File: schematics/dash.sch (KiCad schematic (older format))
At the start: 29 parts, among them J1 BATT_CONN, J2 EXTERNAL_TRIGGER, J3 USB_OTG, SW1 SW_Push, U1 ESP-12E, U2 ch340g, U3 MCP73833, U4 HT7333, Y1 12Mhz

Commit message: [enh] Change capacitor value to match ceramic capacitor availability
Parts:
- removed C1: 470uF, Capacitors_SMD:C_1206_HandSoldering, symbol C
- added C1: 220uF, Capacitors_SMD:C_1206_HandSoldering, symbol C_Small
- C7: footprint Capacitors_Tantalum_SMD:CP_Tantalum_Case-A_EIA-3216-18_Hand -> Capacitors_SMD:C_1206_HandSoldering
- C9: value 470uF -> 220uF; footprint Capacitors_Tantalum_SMD:CP_Tantalum_Case-D_EIA-7343-31_Hand -> Capacitors_SMD:C_1206_HandSoldering
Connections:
- net GND: now also C1.2
- net at C7.2, J1.2 (P2), U3.10 (VBAT)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: now also C1.1
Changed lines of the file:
@@
-$EndComp
-$Comp
-L C C1
-U 1 1 5960EA3A
-P 8800 2150
-F 0 "C1" H 8825 2250 50  0000 L CNN
-F 1 "470uF" H 8825 2050 50  0000 L CNN
-F 2 "Capacitors_SMD:C_1206_HandSoldering" H 8838 2000 50  0001 C CNN
-F 3 "" H 8800 2150 50  0001 C CNN
-	1    8800 2150
-	1    0    0    -1
 $EndComp
 $Comp
@@
 F 0 "C7" V 8250 2000 50  0000 L CNN
 F 1 "1uF" V 8250 2200 50  0000 L CNN
-F 2 "Capacitors_Tantalum_SMD:CP_Tantalum_Case-A_EIA-3216-18_Hand" H 8200 2150 50  0001 C CNN
+F 2 "Capacitors_SMD:C_1206_HandSoldering" H 8200 2150 50  0001 C CNN
 F 3 "" H 8200 2150 50  0001 C CNN
 	1    8200 2150
@@
 P 10000 2150
 F 0 "C9" H 10010 2220 50  0000 L CNN
-F 1 "470uF" H 10010 2070 50  0000 L CNN
-F 2 "Capacitors_Tantalum_SMD:CP_Tantalum_Case-D_EIA-7343-31_Hand" H 10000 2150 50  0001 C CNN
+F 1 "220uF" H 10010 2070 50  0000 L CNN
+F 2 "Capacitors_SMD:C_1206_HandSoldering" H 10000 2150 50  0001 C CNN
 F 3 "" H 10000 2150 50  0001 C CNN
 	1    10000 2150
@@
 Connection ~ 8800 1900
 Wire Wire Line
-	8800 2400 8800 2300
-Wire Wire Line
-	8800 1900 8800 2000
+	8800 2250 8800 2400
+Wire Wire Line
+	8800 1900 8800 2050
 Wire Wire Line
 	5750 4550 5350 4550
@@
 	1    0    0    -1
 $EndComp
+$Comp
+L C_Small C1
+U 1 1 59C67224
+P 8800 2150
+F 0 "C1" H 8810 2220 50  0000 L CNN
+F 1 "220uF" H 8810 2070 50  0000 L CNN
+F 2 "Capacitors_SMD:C_1206_HandSoldering" H 8800 2150 50  0001 C CNN
+F 3 "" H 8800 2150 50  0001 C CNN
+	1    8800 2150
+	1    0    0    -1
+$EndComp

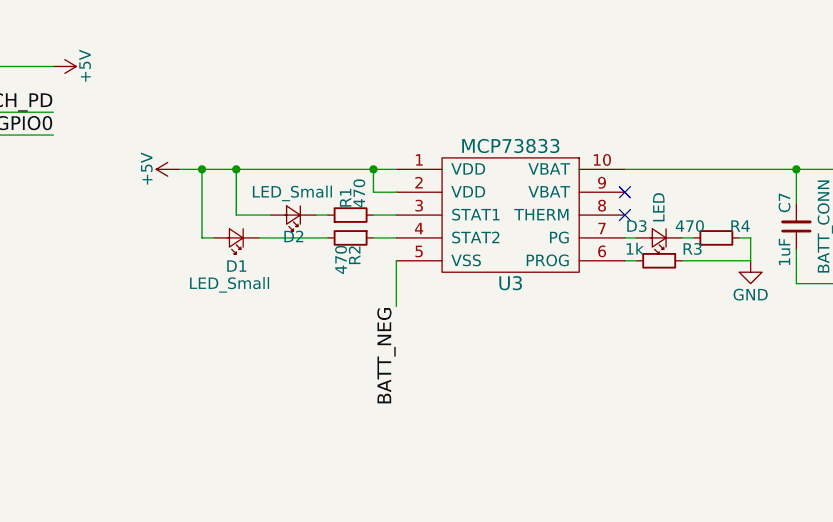
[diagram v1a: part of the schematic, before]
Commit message: [enh] Redesigned project to take less space
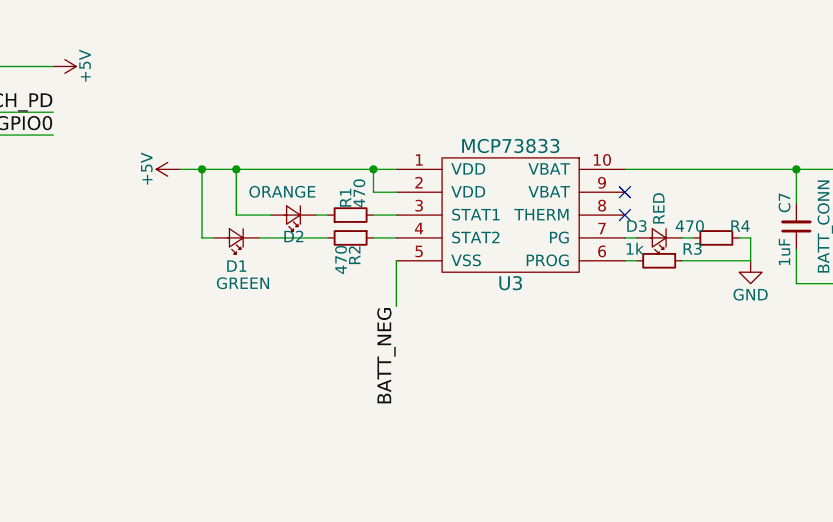
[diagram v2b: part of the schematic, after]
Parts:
- D1: value LED_Small -> GREEN
- D2: value LED_Small -> ORANGE
- D3: value LED -> RED
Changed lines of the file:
@@
 P 6000 2100
 F 0 "D2" H 5950 2225 50  0000 L TNN
-F 1 "LED_Small" H 5825 2000 50  0000 L CNN
+F 1 "ORANGE" H 5900 2000 50  0000 L CNN
 F 2 "LEDs:LED_1206" V 6000 2100 50  0001 C CNN
 F 3 "" V 6000 2100 50  0001 C CNN
@@
 P 5750 2200
 F 0 "D1" H 5700 2325 50  0000 L CNN
-F 1 "LED_Small" H 5600 2400 50  0000 L CNN
+F 1 "GREEN" H 5600 2400 50  0000 L CNN
 F 2 "LEDs:LED_1206" V 5750 2200 50  0001 C CNN
 F 3 "" V 5750 2200 50  0001 C CNN
@@
 P 7600 2200
 F 0 "D3" H 7650 2150 50  0000 L CNN
-F 1 "LED" V 7600 2000 50  0000 L CNN
+F 1 "RED" V 7600 2000 50  0000 L CNN
 F 2 "LEDs:LED_1206" V 7600 2200 50  0001 C CNN
 F 3 "" V 7600 2200 50  0001 C CNN

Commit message: [add] Pinout
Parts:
- added J4, J5: Conn_01x08, Pin_Headers:Pin_Header_Straight_1x08_Pitch2.54mm, symbol Conn_01x08
- U4: footprint TO_SOT_Packages_SMD:SOT89-3_Housing_Handsoldering -> sot:SOT89
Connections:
- net +3V3: now also J4.1 (Pin_1)
- net CH_PD: now also J4.6 (Pin_6)
- net GND: now also J5.8 (Pin_8)
- net GPIO0: now also J5.5 (Pin_5)
- net GPIO15: now also J5.7 (Pin_7)
- net GPIO2: now also J5.6 (Pin_6)
- net RXD: now also J5.2 (Pin_2)
- net TXD: now also J5.1 (Pin_1)
- net GPIO4: now reaches U1.13 (GPIO4)
- net GPIO4: now also J5.4 (Pin_4)
- net GPIO5: now reaches U1.14 (GPIO5)
- net GPIO5: now also J5.3 (Pin_3)
- net ADC: now reaches U1.2 (ADC)
- net ADC: now also J4.7 (Pin_7)
- net GPIO14: now reaches U1.5 (GPIO14)
- net GPIO14: now also J4.4 (Pin_4)
- net GPIO12: now reaches U1.6 (GPIO12)
- net GPIO12: now also J4.3 (Pin_3)
- net GPIO13: now reaches U1.7 (GPIO13)
- net GPIO13: now also J4.2 (Pin_2)
- net WAKE renamed GPIO16
- net GPIO16: now also J4.5 (Pin_5), J4.8 (Pin_8)
- no-connect marks 21 -> 15
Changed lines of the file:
@@
 $EndComp
 Text Label 5350 4650 0    60   ~ 0
-WAKE
+GPIO16
 $Comp
 L CONN_01X02 J2
@@
 NoConn ~ 1600 2150
 NoConn ~ 1200 2350
-Text Label 7850 4350 2    60   ~ 0
+Text Label 7900 4350 2    60   ~ 0
 TXD
-Text Label 7850 4450 2    60   ~ 0
+Text Label 7900 4450 2    60   ~ 0
 RXD
 Text Label 3350 1550 0    60   ~ 0
@@
 F 0 "U4" H 9400 2000 60  0000 C CNN
 F 1 "HT7333" H 9400 2100 60  0000 C CNN
-F 2 "TO_SOT_Packages_SMD:SOT89-3_Housing_Handsoldering" H 9400 1900 60  0001 C CNN
+F 2 "sot:SOT89" H 9400 1900 60  0001 C CNN
 F 3 "" H 9400 1900 60  0001 C CNN
 	1    9400 1900
@@
 Text Label 7900 4750 2    60   ~ 0
 GPIO0
-Text Label 5450 3850 3    60   ~ 0
-WAKE
-NoConn ~ 7550 4550
-NoConn ~ 7550 4650
-NoConn ~ 5750 4750
-NoConn ~ 5750 4850
-NoConn ~ 5750 4950
-NoConn ~ 5750 4450
+Text Label 5550 3850 3    60   ~ 0
+GPIO16
 NoConn ~ 7450 2100
 $Comp
@@
 	5500 1900 6450 1900
 Wire Wire Line
-	5750 5050 5350 5050
+	5350 5050 5750 5050
 Wire Wire Line
 	1600 1750 2600 1750
@@
 Wire Wire Line
 	5200 3950 5200 4350
-Connection ~ 5450 4350
-Wire Wire Line
-	5450 4350 5450 3850
+Connection ~ 5550 4350
+Wire Wire Line
+	5550 4350 5550 3850
 Wire Wire Line
 	5700 4350 5700 4200
@@
 Connection ~ 8800 1900
 Wire Wire Line
-	8800 2250 8800 2400
+	8800 2400 8800 2250
 Wire Wire Line
 	8800 1900 8800 2050
@@
 Connection ~ 3700 2750
 Wire Wire Line
-	3700 2650 3700 2750
+	3700 2750 3700 2650
 Wire Wire Line
 	3150 2750 4350 2750
@@
 Connection ~ 8650 2400
 Wire Wire Line
-	7550 4450 7850 4450
-Wire Wire Line
-	7550 4350 7850 4350
+	7550 4450 7900 4450
+Wire Wire Line
+	7550 4350 7900 4350
 Wire Wire Line
 	4500 4350 4750 4350
@@
 	1    0    0    -1
 $EndComp
+$Comp
+L Conn_01x08 J5
+U 1 1 59CC2428
+P 3850 6450
+F 0 "J5" H 3850 6850 50  0000 C CNN
+F 1 "Conn_01x08" H 3850 5950 50  0000 C CNN
+F 2 "Pin_Headers:Pin_Header_Straight_1x08_Pitch2.54mm" H 3850 6450 50  0001 C CNN
+F 3 "" H 3850 6450 50  0001 C CNN
+	1    3850 6450
+	0    1    1    0
+$EndComp
+$Comp
+L Conn_01x08 J4
+U 1 1 59CC25B5
+P 2600 6450
+F 0 "J4" H 2600 6850 50  0000 C CNN
+F 1 "Conn_01x08" H 2600 5950 50  0000 C CNN
+F 2 "Pin_Headers:Pin_Header_Straight_1x08_Pitch2.54mm" H 2600 6450 50  0001 C CNN
+F 3 "" H 2600 6450 50  0001 C CNN
+	1    2600 6450
+	0    1    1    0
+$EndComp
+Wire Wire Line
+	2200 6250 2200 6000
+Wire Wire Line
+	2300 6250 2300 6000
+Wire Wire Line
+	2400 6250 2400 6000
+Wire Wire Line
+	2500 6250 2500 6000
+Wire Wire Line
+	2600 6250 2600 6000
+Wire Wire Line
+	2700 6250 2700 6000
+Wire Wire Line
+	2800 6250 2800 6000
+Wire Wire Line
+	2900 6250 2900 6000
+Wire Wire Line
+	3450 6250 3450 6000
+Wire Wire Line
+	3550 6250 3550 6000
+Wire Wire Line
+	3650 6250 3650 6000
+Wire Wire Line
+	3750 6250 3750 6000
+Wire Wire Line
+	3850 6250 3850 6000
+Wire Wire Line
+	3950 6250 3950 6000
+Wire Wire Line
+	4050 6250 4050 6000
+Wire Wire Line
+	4150 6250 4150 6000
+Text Label 2200 6000 1    60   ~ 0
+REST
+Text Label 2300 6000 1    60   ~ 0
+ADC
+Text Label 2400 6000 1    60   ~ 0
+CH_PD
+Text Label 2500 6000 1    60   ~ 0
+GPIO16
+Text Label 2600 6000 1    60   ~ 0
+GPIO14
+Text Label 2700 6000 1    60   ~ 0
+GPIO12
+Text Label 2800 6000 1    60   ~ 0
+GPIO13
+Text Label 2900 6000 1    60   ~ 0
+VCC
+Text Label 4150 6000 1    60   ~ 0
+TXD
+Text Label 4050 6000 1    60   ~ 0
+RXD
+Text Label 3950 6000 1    60   ~ 0
+GPIO5
+Text Label 3850 6000 1    60   ~ 0
+GPIO4
+Text Label 3750 6000 1    60   ~ 0
+GPIO0
+Text Label 3650 6000 1    60   ~ 0
+GPIO2
+Text Label 3550 6000 1    60   ~ 0
+GPIO15
+Text Label 3450 6000 1    60   ~ 0
+GND
+Wire Wire Line
+	7550 4650 7900 4650
+Wire Wire Line
+	7550 4550 7900 4550
+Wire Wire Line
+	5350 4450 5750 4450
+Wire Wire Line
+	5750 4750 5350 4750
+Wire Wire Line
+	5750 4850 5350 4850
+Wire Wire Line
+	5750 4950 5350 4950
+Text Label 5350 4450 0    60   ~ 0
+ADC
+Text Label 5350 4750 0    60   ~ 0
+GPIO14
+Text Label 5350 4850 0    60   ~ 0
+GPIO12
+Text Label 5350 4950 0    60   ~ 0
+GPIO13
+Text Label 7900 4550 2    60   ~ 0
+GPIO5
+Text Label 7900 4650 2    60   ~ 0
+GPIO4
+Wire Wire Line
+	5350 4350 5350 3850
+Connection ~ 5350 4350
+Text Label 5350 3850 3    60   ~ 0
+REST
+Text Label 5350 5050 0    60   ~ 0
+VCC
 $EndSCHEMATC

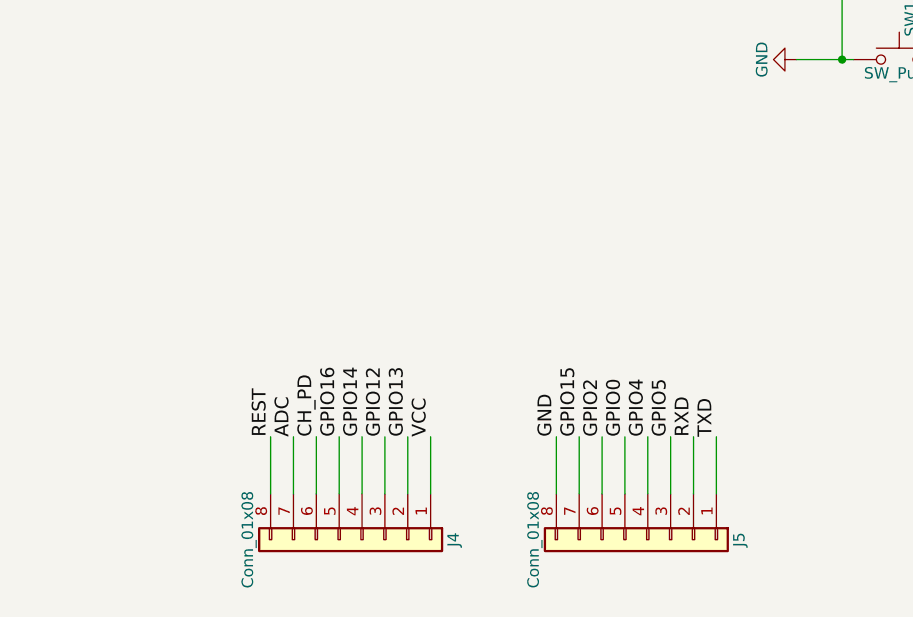
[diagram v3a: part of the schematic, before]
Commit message: [enh] Add 3d models + better external trigger pad
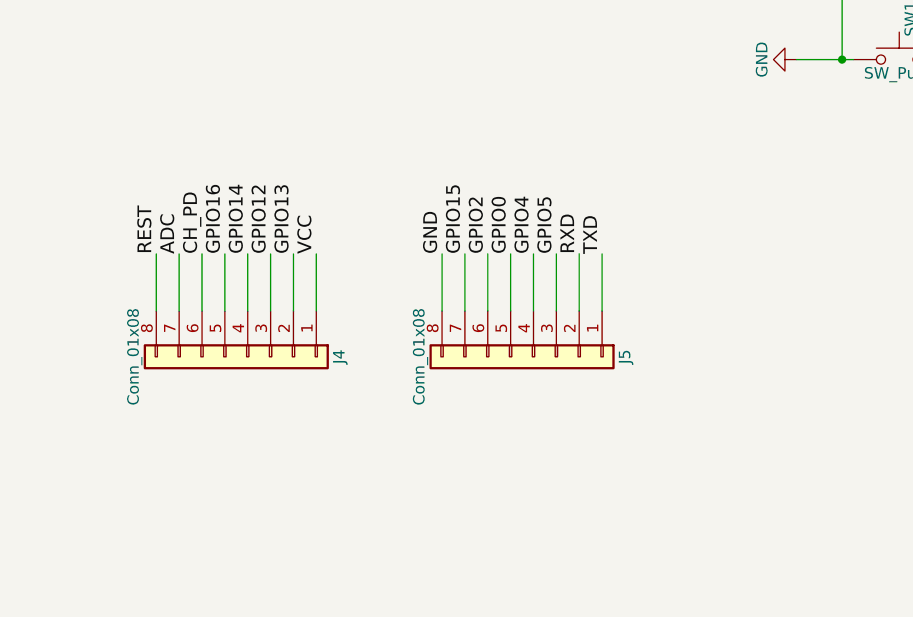
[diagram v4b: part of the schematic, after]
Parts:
- J1: footprint Connectors_JST:JST_ACH_BM02B-ACHSS_02x1.20mm_Angled -> Connectors_JST:JST_SH_SM02B-SRSS-TB_02x1.00mm_Angled
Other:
- moved on the sheet: J4, J5
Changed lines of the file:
@@
 F 0 "J1" H 8450 2300 50  0000 C CNN
 F 1 "BATT_CONN" V 8550 2150 50  0000 C TNN
-F 2 "Connectors_JST:JST_ACH_BM02B-ACHSS_02x1.20mm_Angled" H 8450 2150 50  0001 C CNN
+F 2 "Connectors_JST:JST_SH_SM02B-SRSS-TB_02x1.00mm_Angled" H 8450 2150 50  0001 C CNN
 F 3 "" H 8450 2150 50  0001 C CNN
 	1    8450 2150
@@
 L Conn_01x08 J5
 U 1 1 59CC2428
-P 3850 6450
-F 0 "J5" H 3850 6850 50  0000 C CNN
-F 1 "Conn_01x08" H 3850 5950 50  0000 C CNN
-F 2 "Pin_Headers:Pin_Header_Straight_1x08_Pitch2.54mm" H 3850 6450 50  0001 C CNN
-F 3 "" H 3850 6450 50  0001 C CNN
-	1    3850 6450
+P 3350 5650
+F 0 "J5" H 3350 6050 50  0000 C CNN
+F 1 "Conn_01x08" H 3350 5150 50  0000 C CNN
+F 2 "Pin_Headers:Pin_Header_Straight_1x08_Pitch2.54mm" H 3350 5650 50  0001 C CNN
+F 3 "" H 3350 5650 50  0001 C CNN
+	1    3350 5650
 	0    1    1    0
 $EndComp
@@
 L Conn_01x08 J4
 U 1 1 59CC25B5
-P 2600 6450
-F 0 "J4" H 2600 6850 50  0000 C CNN
-F 1 "Conn_01x08" H 2600 5950 50  0000 C CNN
-F 2 "Pin_Headers:Pin_Header_Straight_1x08_Pitch2.54mm" H 2600 6450 50  0001 C CNN
-F 3 "" H 2600 6450 50  0001 C CNN
-	1    2600 6450
-	0    1    1    0
-$EndComp
-Wire Wire Line
-	2200 6250 2200 6000
-Wire Wire Line
-	2300 6250 2300 6000
-Wire Wire Line
-	2400 6250 2400 6000
-Wire Wire Line
-	2500 6250 2500 6000
-Wire Wire Line
-	2600 6250 2600 6000
-Wire Wire Line
-	2700 6250 2700 6000
-Wire Wire Line
-	2800 6250 2800 6000
-Wire Wire Line
-	2900 6250 2900 6000
-Wire Wire Line
-	3450 6250 3450 6000
-Wire Wire Line
-	3550 6250 3550 6000
-Wire Wire Line
-	3650 6250 3650 6000
-Wire Wire Line
-	3750 6250 3750 6000
-Wire Wire Line
-	3850 6250 3850 6000
-Wire Wire Line
-	3950 6250 3950 6000
-Wire Wire Line
-	4050 6250 4050 6000
-Wire Wire Line
-	4150 6250 4150 6000
-Text Label 2200 6000 1    60   ~ 0
+P 2100 5650
+F 0 "J4" H 2100 6050 50  0000 C CNN
+F 1 "Conn_01x08" H 2100 5150 50  0000 C CNN
+F 2 "Pin_Headers:Pin_Header_Straight_1x08_Pitch2.54mm" H 2100 5650 50  0001 C CNN
+F 3 "" H 2100 5650 50  0001 C CNN
+	1    2100 5650
+	0    1    1    0
+$EndComp
+Wire Wire Line
+	1700 5450 1700 5200
+Wire Wire Line
+	1800 5450 1800 5200
+Wire Wire Line
+	1900 5450 1900 5200
+Wire Wire Line
+	2000 5450 2000 5200
+Wire Wire Line
+	2100 5450 2100 5200
+Wire Wire Line
+	2200 5450 2200 5200
+Wire Wire Line
+	2300 5450 2300 5200
+Wire Wire Line
+	2400 5450 2400 5200
+Wire Wire Line
+	2950 5450 2950 5200
+Wire Wire Line
+	3050 5450 3050 5200
+Wire Wire Line
+	3150 5450 3150 5200
+Wire Wire Line
+	3250 5450 3250 5200
+Wire Wire Line
+	3350 5450 3350 5200
+Wire Wire Line
+	3450 5450 3450 5200
+Wire Wire Line
+	3550 5450 3550 5200
+Wire Wire Line
+	3650 5450 3650 5200
+Text Label 1700 5200 1    60   ~ 0
 REST
-Text Label 2300 6000 1    60   ~ 0
+Text Label 1800 5200 1    60   ~ 0
 ADC
-Text Label 2400 6000 1    60   ~ 0
+Text Label 1900 5200 1    60   ~ 0
 CH_PD
-Text Label 2500 6000 1    60   ~ 0
+Text Label 2000 5200 1    60   ~ 0
 GPIO16
-Text Label 2600 6000 1    60   ~ 0
+Text Label 2100 5200 1    60   ~ 0
 GPIO14
-Text Label 2700 6000 1    60   ~ 0
+Text Label 2200 5200 1    60   ~ 0
 GPIO12
-Text Label 2800 6000 1    60   ~ 0
+Text Label 2300 5200 1    60   ~ 0
 GPIO13
-Text Label 2900 6000 1    60   ~ 0
+Text Label 2400 5200 1    60   ~ 0
 VCC
-Text Label 4150 6000 1    60   ~ 0
+Text Label 3650 5200 1    60   ~ 0
 TXD
-Text Label 4050 6000 1    60   ~ 0
+Text Label 3550 5200 1    60   ~ 0
 RXD
-Text Label 3950 6000 1    60   ~ 0
+Text Label 3450 5200 1    60   ~ 0
 GPIO5
-Text Label 3850 6000 1    60   ~ 0
+Text Label 3350 5200 1    60   ~ 0
 GPIO4
-Text Label 3750 6000 1    60   ~ 0
+Text Label 3250 5200 1    60   ~ 0
 GPIO0
-Text Label 3650 6000 1    60   ~ 0
+Text Label 3150 5200 1    60   ~ 0
 GPIO2
-Text Label 3550 6000 1    60   ~ 0
+Text Label 3050 5200 1    60   ~ 0
 GPIO15
-Text Label 3450 6000 1    60   ~ 0
+Text Label 2950 5200 1    60   ~ 0
 GND
 Wire Wire Line

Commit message: [fix] Change crystal footprint to match availability
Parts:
- J2: footprint Connectors:GS2 -> Pin_Headers:Pin_Header_Straight_1x02_Pitch2.54mm_SMD_Pin1Left
- J3: footprint Connectors:USB_Micro-B -> Connectors_USB:USB_Micro-B_Molex_47346-0001
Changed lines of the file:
@@
 F 0 "J2" H 4950 3900 50  0000 C CNN
 F 1 "EXTERNAL_TRIGGER" V 5050 3750 50  0000 C CNN
-F 2 "Connectors:GS2" H 4950 3750 50  0001 C CNN
+F 2 "Pin_Headers:Pin_Header_Straight_1x02_Pitch2.54mm_SMD_Pin1Left" H 4950 3750 50  0001 C CNN
 F 3 "" H 4950 3750 50  0001 C CNN
 	1    4950 3750
@@
 F 0 "J3" H 1100 2400 50  0000 L CNN
 F 1 "USB_OTG" H 1100 2300 50  0000 L CNN
-F 2 "Connectors:USB_Micro-B" H 1450 1900 50  0001 C CNN
+F 2 "Connectors_USB:USB_Micro-B_Molex_47346-0001" H 1450 1900 50  0001 C CNN
 F 3 "" H 1450 1900 50  0001 C CNN
 	1    1300 1950

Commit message: [add] Forgot to update sch
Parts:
- Y1: footprint Crystals:Crystal_SMD_2012-2pin_2.0x1.2mm_HandSoldering -> Crystals:Crystal_SMD_3225-4pin_3.2x2.5mm_HandSoldering
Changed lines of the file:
@@
 F 0 "Y1" H 3550 2400 50  0000 C CNN
 F 1 "12Mhz" H 3550 2100 50  0000 C CNN
-F 2 "Crystals:Crystal_SMD_2012-2pin_2.0x1.2mm_HandSoldering" H 3550 2250 50  0001 C CNN
+F 2 "Crystals:Crystal_SMD_3225-4pin_3.2x2.5mm_HandSoldering" H 3550 2250 50  0001 C CNN
 F 3 "" H 3550 2250 50  0001 C CNN
 	1    3550 2250
